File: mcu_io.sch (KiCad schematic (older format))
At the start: 15 parts

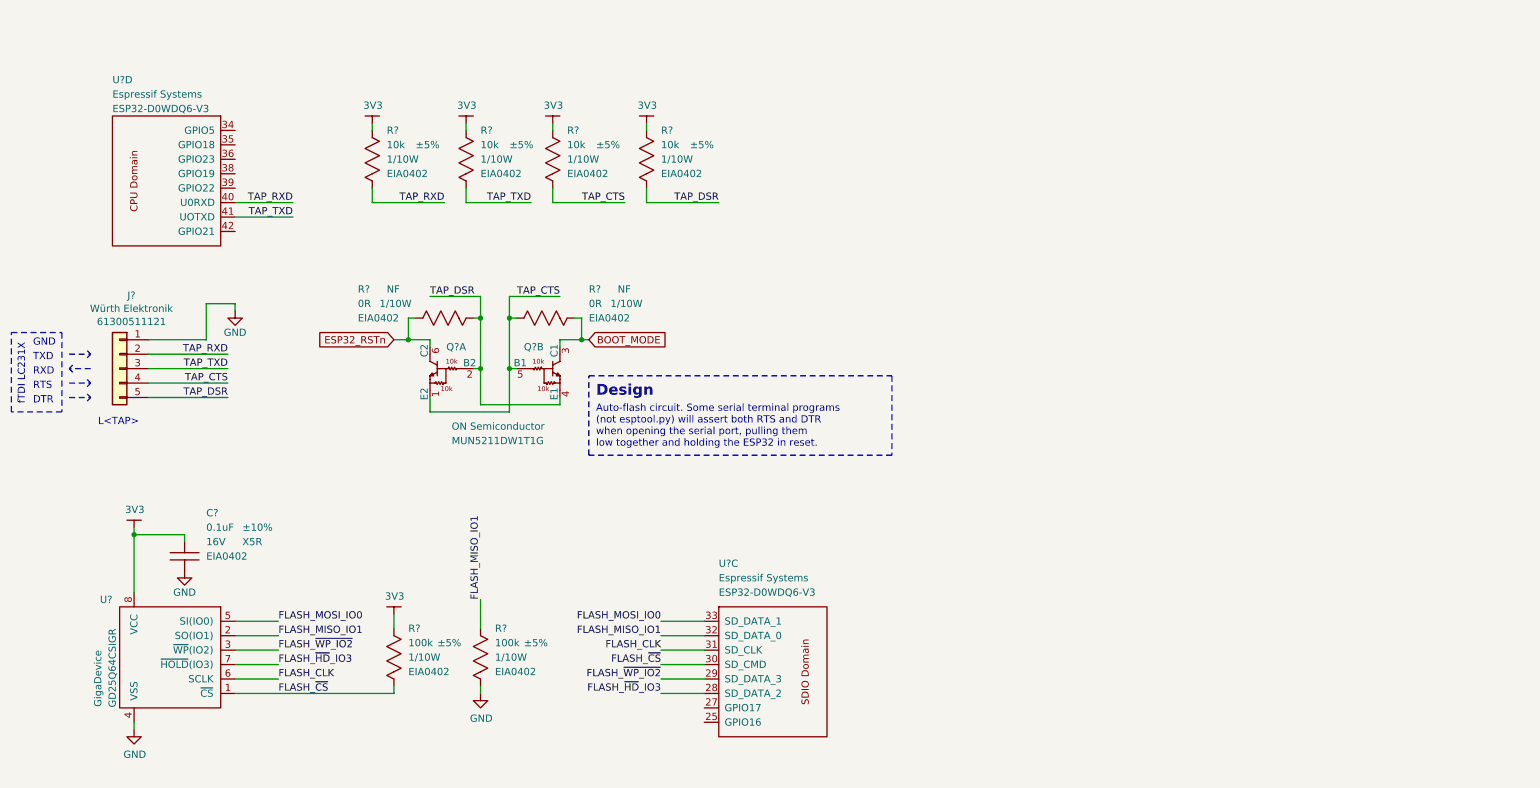
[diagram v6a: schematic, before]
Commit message: Fix Boot Mode LED circuit (add PNP drive); add 2x BiColour general-purpose LED's.
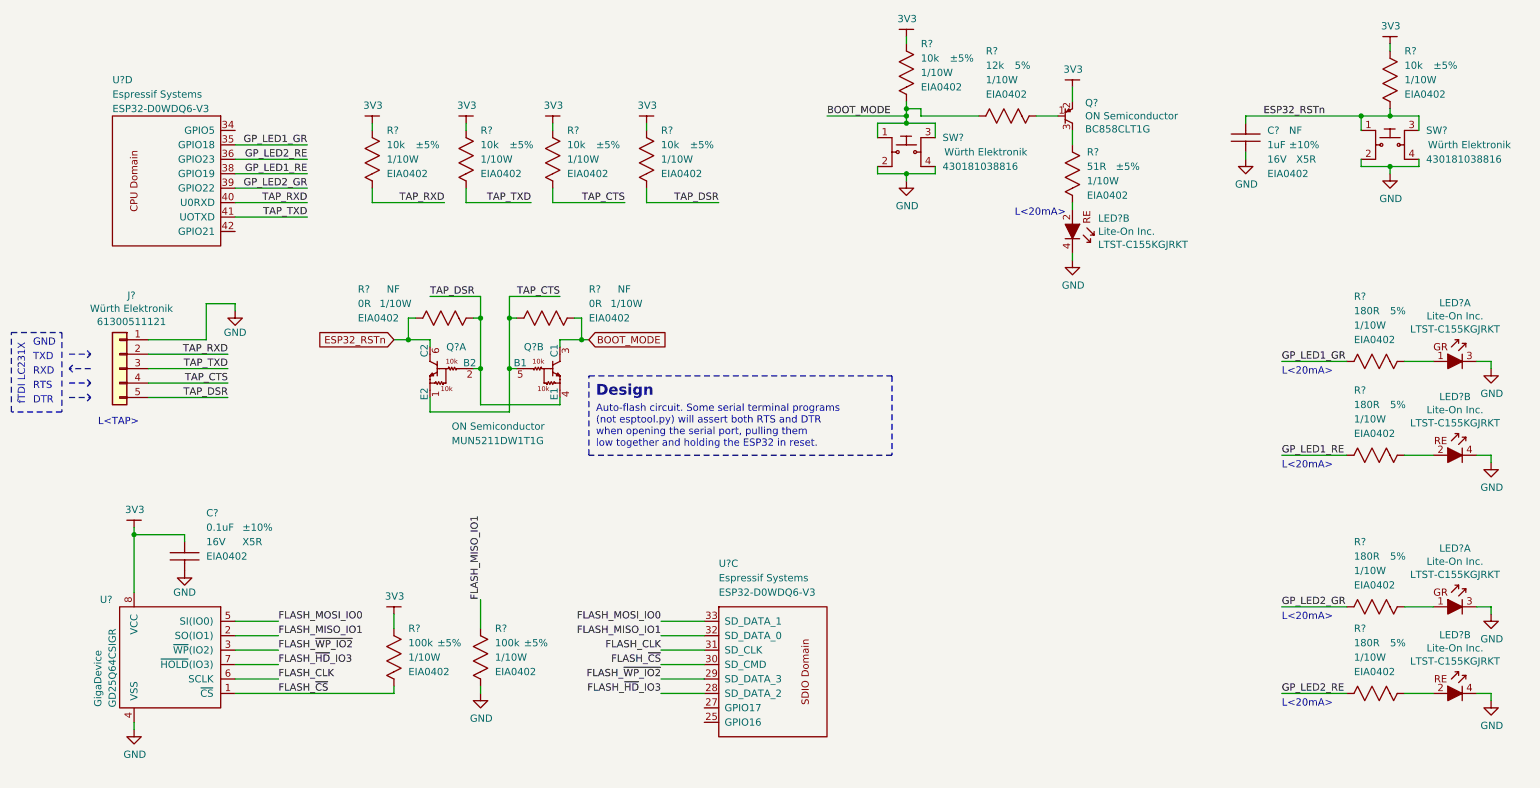
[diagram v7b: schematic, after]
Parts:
- added C?: CAP-EIA0402, footprints_generic:CAPC100X50X55L30N, symbol gz_Ceramic-Capacitors:CAP-EIA0402
- added LED? (x5): LiteOn-LTST-C155KGJRKT, footprints:LiteOn-LTST-C155_LEDCAV4P138_270X320X110L50X90N, symbol gz_LED-Indication-Discrete:LiteOn-LTST-C155KGJRKT
- added Q?: ON-Semi_BC858CLT1G, footprints:ON-Semi-BC858CLT1G_SOT23-3P85_237X111L42X43N, symbol gz_Transistors-Bipolar-BJT-Single:ON-Semi_BC858CLT1G
- added R? (x8): RES-EIA0402, footprints_generic:RESC100X50X40L25NN, symbol gz_Chip-Resistors-Surface-Mount:RES-EIA0402
- added SW? (x2): WE-430181038816, footprints:WE-430181038816_SWSOFL4P150_450X750X380L150X70N, symbol gz_Tactile-Switches:WE-430181038816
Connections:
- net +3V3: now also Q?.2 (E), R?.1, R?.1
- net BOOT_MODE: now also R?.1, R?.2, SW?.1, SW?.3
- net ESP32_RSTn: now also C?.1, R?.2, SW?.1, SW?.3
- net GND: now also C?.2, LED?.3 (C), LED?.3 (C), LED?.4 (C), LED?.4 (C), LED?.4 (C), SW?.2, SW?.2, SW?.4, SW?.4
- net GP_LED1_GR: now reaches U?.35 (GPIO18)
- net GP_LED1_GR: now also R?.1
- net GP_LED2_RE: now reaches U?.36 (GPIO23)
- net GP_LED2_RE: now also R?.1
- net GP_LED1_RE: now reaches U?.38 (GPIO19)
- net GP_LED1_RE: now also R?.1
- net GP_LED2_GR: now reaches U?.39 (GPIO22)
- net GP_LED2_GR: now also R?.1
- new net: Q?.1 (B), R?.2
- new net: Q?.3 (C), R?.1
- new net: LED?.2 (A), R?.2 (x3)
- new net: LED?.1 (A), R?.2 (x2)
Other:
- note added: "L<20mA>"

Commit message: Add general purpose tact switches.
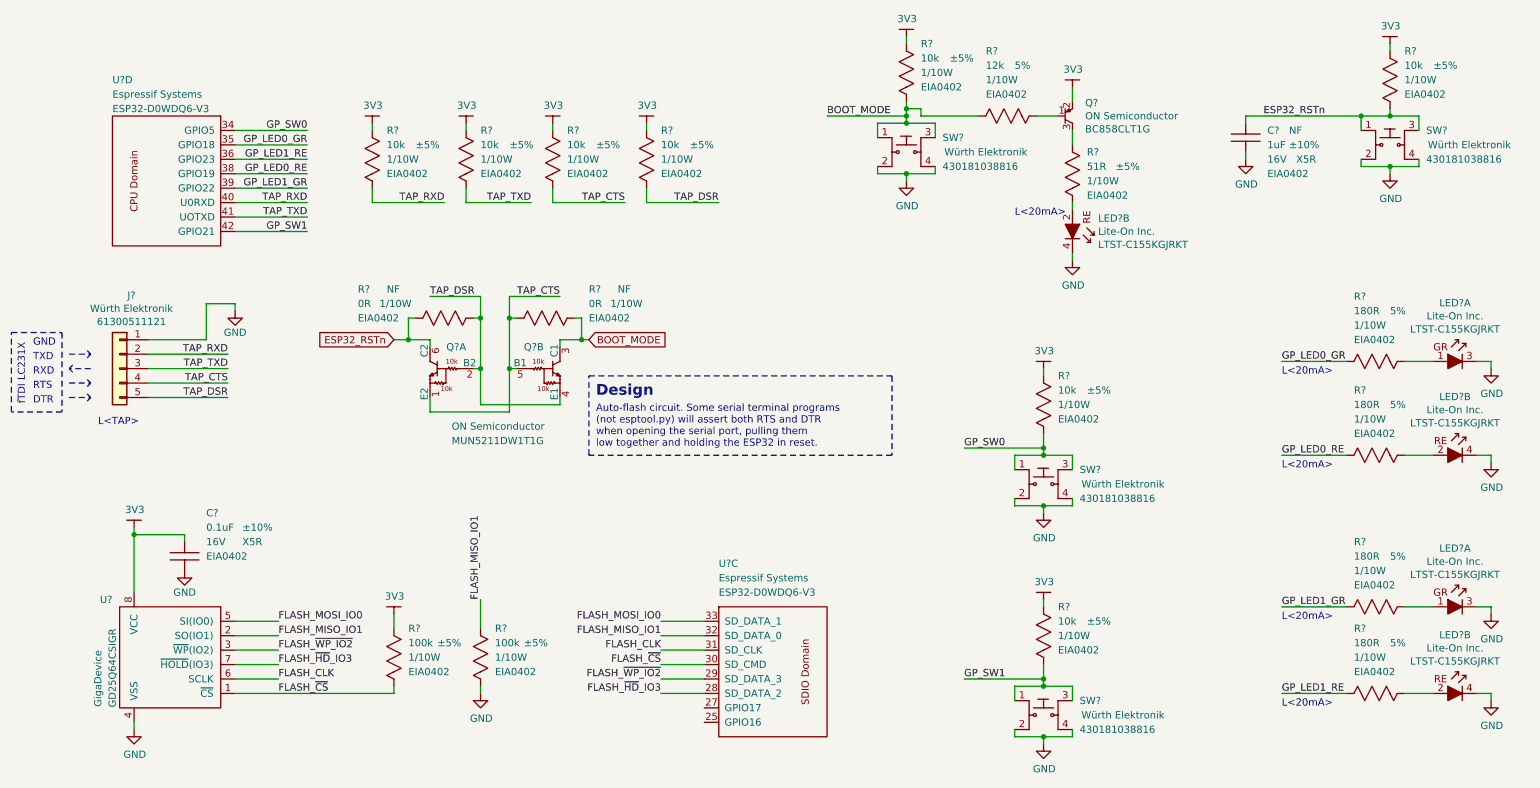
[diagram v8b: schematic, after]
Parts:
- added R? (x2): RES-EIA0402, footprints_generic:RESC100X50X40L25NN, symbol gz_Chip-Resistors-Surface-Mount:RES-EIA0402
- added SW? (x2): WE-430181038816, footprints:WE-430181038816_SWSOFL4P150_450X750X380L150X70N, symbol gz_Tactile-Switches:WE-430181038816
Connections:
- net GP_LED2_GR is gone; now on net GP_LED1_GR: R?.1, U?.39 (GPIO22)
- net GP_LED2_RE is gone; now on net GP_LED1_RE: R?.1, U?.36 (GPIO23)
- net +3V3: now also R?.1, R?.1
- net GND: now also SW?.2, SW?.2, SW?.4, SW?.4
- net GP_LED1_GR: no longer R?.1, U?.35 (GPIO18)
- net GP_LED1_RE: no longer R?.1, U?.38 (GPIO19)
- net GP_SW0: now reaches U?.34 (GPIO5)
- net GP_SW0: now also R?.2, SW?.1, SW?.3
- net GP_SW1: now reaches U?.42 (GPIO21)
- net GP_SW1: now also R?.2, SW?.1, SW?.3
- new net GP_LED0_GR: R?.1, U?.35 (GPIO18)
- new net GP_LED0_RE: R?.1, U?.38 (GPIO19)
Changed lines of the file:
@@
 	9850 5300 9400 5300
 Text Label 9400 3000 0    50   ~ 0
+GP_LED0_GR
+Text Label 9400 3650 0    50   ~ 0
+GP_LED0_RE
+Text Label 9400 5300 0    50   ~ 0
+GP_LED1_RE
+Text Label 9400 4700 0    50   ~ 0
 GP_LED1_GR
-Text Label 9400 3650 0    50   ~ 0
-GP_LED1_RE
-Text Label 9400 5300 0    50   ~ 0
-GP_LED2_RE
-Text Label 9400 4700 0    50   ~ 0
-GP_LED2_GR
 Wire Wire Line
 	2150 1500 2650 1500
@@
 	2150 1800 2650 1800
 Text Label 2650 1500 2    50   ~ 0
+GP_LED0_GR
+Text Label 2650 1700 2    50   ~ 0
+GP_LED0_RE
+Text Label 2650 1800 2    50   ~ 0
 GP_LED1_GR
-Text Label 2650 1700 2    50   ~ 0
+Text Label 2650 1600 2    50   ~ 0
 GP_LED1_RE
-Text Label 2650 1800 2    50   ~ 0
-GP_LED2_GR
-Text Label 2650 1600 2    50   ~ 0
-GP_LED2_RE
 Text Notes 9400 3750 0    50   ~ 0
 L<20mA>
@@
 Text Notes 7550 2000 0    50   ~ 0
 L<20mA>
+$Comp
+L gz_Tactile-Switches:WE-430181038816 SW?
+U 1 1 6074B4B8
+P 7750 3850
+AR Path="/60330427/6074B4B8" Ref="SW?"  Part="1"
+AR Path="/606CDE66/6074B4B8" Ref="SW?"  Part="1"
+F 0 "SW?" H 8000 3950 50  0000 L CNN
+F 1 "WE-430181038816" H 8400 4550 50  0001 L CNN
+F 2 "footprints:WE-430181038816_SWSOFL4P150_450X750X380L150X70N" H 8400 4450 50  0001 L CNN
+F 3 "https://katalog.we-online.de/em/datasheet/430181038816.pdf" H 7950 4150 50  0001 L CNN
+F 4 "Digikey" H 8400 4350 50  0001 L CNN "Vendor"
+F 5 "732-7003-1-ND" H 8800 4350 50  0001 L CNN "Vendor_PN"
+F 6 "Würth Elektronik" H 8300 3850 50  0000 C CNN "Manufacturer"
+F 7 "430181038816" H 8000 3750 50  0000 L CNN "MPN"
+F 8 "Switches" H 8400 4250 50  0001 L CNN "Category"
+F 9 "Tactile Switches" H 8400 4150 50  0001 L CNN "Family"
+F 10 "Yes" H 7900 4100 50  0001 L CNN "Fit"
+	1    7750 3850
+	1    0    0    -1
+$EndComp
+Wire Wire Line
+	7550 3950 7550 4000
+Wire Wire Line
+	7950 4000 7950 3950
+$Comp
+L gz_Power-Symbols:GND #PWR?
+U 1 1 6074BA4C
+P 7750 4050
+AR Path="/60330427/6074BA4C" Ref="#PWR?"  Part="1"
+AR Path="/606CDE66/6074BA4C" Ref="#PWR?"  Part="1"
+F 0 "#PWR?" H 7750 3800 50  0001 C CNN
+F 1 "GND" H 7755 3877 50  0000 C CNN
+F 2 "" H 7750 4050 50  0001 C CNN
+F 3 "" H 7750 4050 50  0001 C CNN
+	1    7750 4050
+	1    0    0    -1
+$EndComp
+$Comp
+L gz_Chip-Resistors-Surface-Mount:RES-EIA0402 R?
+U 1 1 6074BA62
+P 7750 3300
+AR Path="/60330427/6074BA62" Ref="R?"  Part="1"
+AR Path="/606CDE66/6074BA62" Ref="R?"  Part="1"
+F 0 "R?" V 7550 3400 50  0000 L CNN
+F 1 "RES-EIA0402" H 8550 4200 50  0001 L CNN
+F 2 "footprints_generic:RESC100X50X40L25NN" H 4450 7650 50  0001 L CNN
+F 3 "${PANASONIC_GP_CHIP_RES_BASE}ERJ2GEJ103X" H 4450 7750 50  0001 L CNN
+F 4 "Digikey" H 7750 3300 50  0001 L CNN "Vendor"
+F 5 "P10KJCT-ND" H 7750 3300 50  0001 L CNN "Vendor_PN"
+F 6 "Panasonic Electronic Components" H 8550 4000 50  0001 L CNN "Manufacturer"
+F 7 "ERJ2GEJ103X" H 8550 3900 50  0001 L CNN "MPN"
+F 8 "Resistors" H 4450 8050 50  0001 L CNN "Category"
+F 9 "Chip Resistor - Surface Mount" H 4450 8150 50  0001 L CNN "Family"
+F 10 "Yes" H 7750 3300 50  0001 C CNN "Fit"
+F 11 "10k" V 7650 3400 50  0000 L CNN "Resistance"
+F 12 "±5%" V 7650 3600 50  0000 L CNN "Tolerance"
+F 13 "1/10W" V 7750 3400 50  0000 L CNN "Power"
+F 14 "N/A" H 7750 3515 50  0001 L CNN "Voltage"
+F 15 "EIA0402" V 7850 3400 50  0000 L CNN "Package"
+	1    7750 3300
+	0    1    1    0
+$EndComp
+Wire Wire Line
+	7550 3750 7550 3650
+Wire Wire Line
+	7950 3650 7950 3750
+Wire Wire Line
+	7550 3650 7750 3650
+Connection ~ 7750 3650
+Wire Wire Line
+	7750 3650 7950 3650
+Wire Wire Line
+	7750 3050 7750 3100
+$Comp
+L gz_Power-Symbols:3V3 #PWR?
+U 1 1 6074BA72
+P 7750 3050
+AR Path="/60330427/6074BA72" Ref="#PWR?"  Part="1"
+AR Path="/606CDE66/6074BA72" Ref="#PWR?"  Part="1"
+F 0 "#PWR?" H 7900 3000 50  0001 C CNN
+F 1 "3V3" H 7755 3173 50  0000 C CNN
+F 2 "" H 7750 3050 50  0001 C CNN
+F 3 "" H 7750 3050 50  0001 C CNN
+	1    7750 3050
+	1    0    0    -1
+$EndComp
+Wire Wire Line
+	7550 4000 7750 4000
+Wire Wire Line
+	7750 4000 7750 4050
+Connection ~ 7750 4000
+Wire Wire Line
+	7750 4000 7950 4000
+Text Label 7200 3600 0    50   ~ 0
+GP_SW0
+Connection ~ 7750 3600
+Wire Wire Line
+	7750 3600 7200 3600
+Wire Wire Line
+	7750 3600 7750 3650
+Wire Wire Line
+	7750 3500 7750 3600
+$Comp
+L gz_Tactile-Switches:WE-430181038816 SW?
+U 1 1 6076036F
+P 7750 5450
+AR Path="/60330427/6076036F" Ref="SW?"  Part="1"
+AR Path="/606CDE66/6076036F" Ref="SW?"  Part="1"
+F 0 "SW?" H 8000 5550 50  0000 L CNN
+F 1 "WE-430181038816" H 8400 6150 50  0001 L CNN
+F 2 "footprints:WE-430181038816_SWSOFL4P150_450X750X380L150X70N" H 8400 6050 50  0001 L CNN
+F 3 "https://katalog.we-online.de/em/datasheet/430181038816.pdf" H 7950 5750 50  0001 L CNN
+F 4 "Digikey" H 8400 5950 50  0001 L CNN "Vendor"
+F 5 "732-7003-1-ND" H 8800 5950 50  0001 L CNN "Vendor_PN"
+F 6 "Würth Elektronik" H 8300 5450 50  0000 C CNN "Manufacturer"
+F 7 "430181038816" H 8000 5350 50  0000 L CNN "MPN"
+F 8 "Switches" H 8400 5850 50  0001 L CNN "Category"
+F 9 "Tactile Switches" H 8400 5750 50  0001 L CNN "Family"
+F 10 "Yes" H 7900 5700 50  0001 L CNN "Fit"
+	1    7750 5450
+	1    0    0    -1
+$EndComp
+Wire Wire Line
+	7550 5550 7550 5600
+Wire Wire Line
+	7950 5600 7950 5550
+$Comp
+L gz_Power-Symbols:GND #PWR?
+U 1 1 60760377
+P 7750 5650
+AR Path="/60330427/60760377" Ref="#PWR?"  Part="1"
+AR Path="/606CDE66/60760377" Ref="#PWR?"  Part="1"
+F 0 "#PWR?" H 7750 5400 50  0001 C CNN
+F 1 "GND" H 7755 5477 50  0000 C CNN
+F 2 "" H 7750 5650 50  0001 C CNN
+F 3 "" H 7750 5650 50  0001 C CNN
+	1    7750 5650
+	1    0    0    -1
+$EndComp
+$Comp
+L gz_Chip-Resistors-Surface-Mount:RES-EIA0402 R?
+U 1 1 60760389
+P 7750 4900
+AR Path="/60330427/60760389" Ref="R?"  Part="1"
+AR Path="/606CDE66/60760389" Ref="R?"  Part="1"
+F 0 "R?" V 7550 5000 50  0000 L CNN
+F 1 "RES-EIA0402" H 8550 5800 50  0001 L CNN
+F 2 "footprints_generic:RESC100X50X40L25NN" H 4450 9250 50  0001 L CNN
+F 3 "${PANASONIC_GP_CHIP_RES_BASE}ERJ2GEJ103X" H 4450 9350 50  0001 L CNN
+F 4 "Digikey" H 7750 4900 50  0001 L CNN "Vendor"
+F 5 "P10KJCT-ND" H 7750 4900 50  0001 L CNN "Vendor_PN"
+F 6 "Panasonic Electronic Components" H 8550 5600 50  0001 L CNN "Manufacturer"
+F 7 "ERJ2GEJ103X" H 8550 5500 50  0001 L CNN "MPN"
+F 8 "Resistors" H 4450 9650 50  0001 L CNN "Category"
+F 9 "Chip Resistor - Surface Mount" H 4450 9750 50  0001 L CNN "Family"
+F 10 "Yes" H 7750 4900 50  0001 C CNN "Fit"
+F 11 "10k" V 7650 5000 50  0000 L CNN "Resistance"
+F 12 "±5%" V 7650 5200 50  0000 L CNN "Tolerance"
+F 13 "1/10W" V 7750 5000 50  0000 L CNN "Power"
+F 14 "N/A" H 7750 5115 50  0001 L CNN "Voltage"
+F 15 "EIA0402" V 7850 5000 50  0000 L CNN "Package"
+	1    7750 4900
+	0    1    1    0
+$EndComp
+Wire Wire Line
+	7550 5350 7550 5250
+Wire Wire Line
+	7950 5250 7950 5350
+Wire Wire Line
+	7550 5250 7750 5250
+Connection ~ 7750 5250
+Wire Wire Line
+	7750 5250 7950 5250
+Wire Wire Line
+	7750 4650 7750 4700
+$Comp
+L gz_Power-Symbols:3V3 #PWR?
+U 1 1 60760395
+P 7750 4650
+AR Path="/60330427/60760395" Ref="#PWR?"  Part="1"
+AR Path="/606CDE66/60760395" Ref="#PWR?"  Part="1"
+F 0 "#PWR?" H 7900 4600 50  0001 C CNN
+F 1 "3V3" H 7755 4773 50  0000 C CNN
+F 2 "" H 7750 4650 50  0001 C CNN
+F 3 "" H 7750 4650 50  0001 C CNN
+	1    7750 4650
+	1    0    0    -1
+$EndComp
+Wire Wire Line
+	7550 5600 7750 5600
+Wire Wire Line
+	7750 5600 7750 5650
+Connection ~ 7750 5600
+Wire Wire Line
+	7750 5600 7950 5600
+Text Label 7200 5200 0    50   ~ 0
+GP_SW1
+Connection ~ 7750 5200
+Wire Wire Line
+	7750 5200 7200 5200
+Wire Wire Line
+	7750 5200 7750 5250
+Wire Wire Line
+	7750 5100 7750 5200
+Text Label 2650 1400 2    50   ~ 0
+GP_SW0
+Text Label 2650 2100 2    50   ~ 0
+GP_SW1
+Wire Wire Line
+	2150 2100 2650 2100
+Wire Wire Line
+	2150 1400 2650 1400
 $EndSCHEMATC
